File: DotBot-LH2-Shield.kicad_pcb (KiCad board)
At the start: 4 copper layers, 29 x 27 mm, 23 parts, among them J1 Conn_01x04, J2 Conn_01x10, J3 Conn_01x10, Q1 NX6008NBKWX, Q2 NX6008NBKWX, Q3 NX6008NBKWX, U1 ISM330DHCXTR, U2 TS4231, U4 LIS3MDL

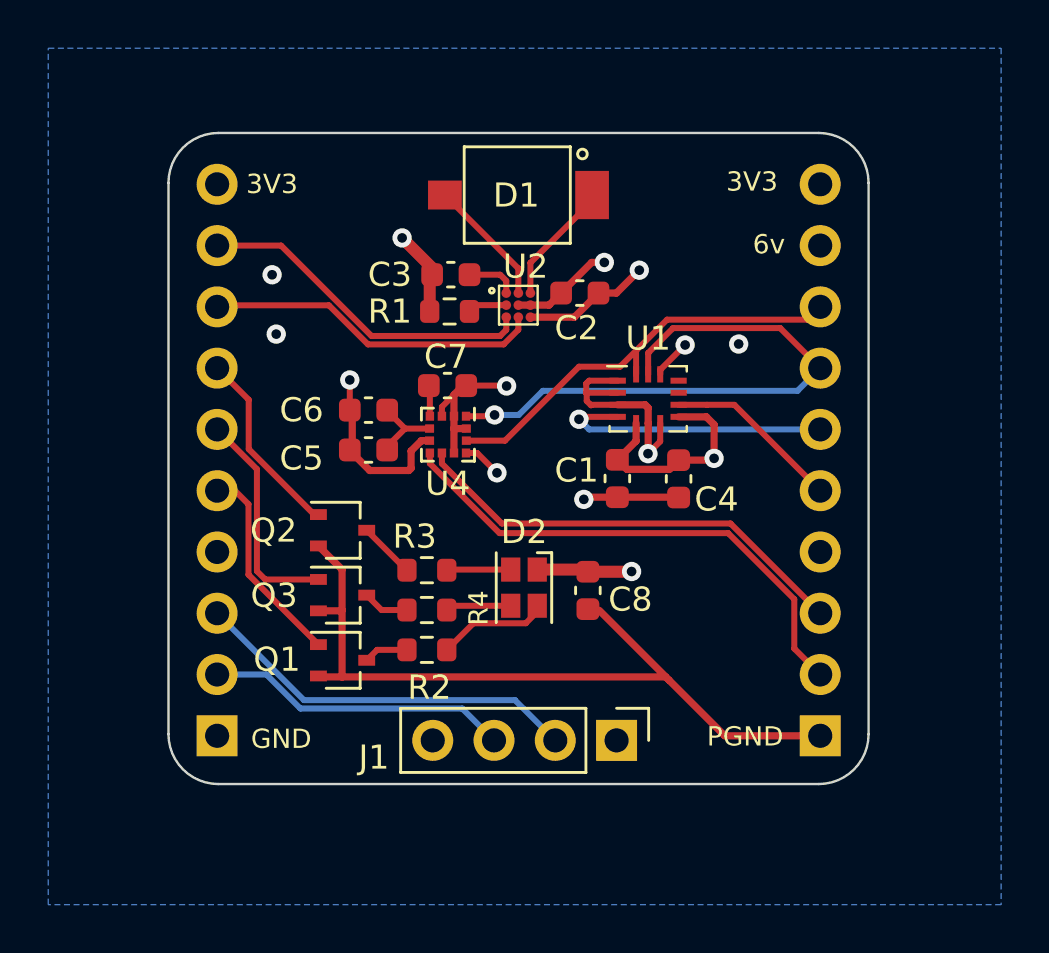
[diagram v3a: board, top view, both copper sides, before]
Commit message: DotBot-LH2-Shield: cleanup silkscreen labels, remove remaining useless stitching vias
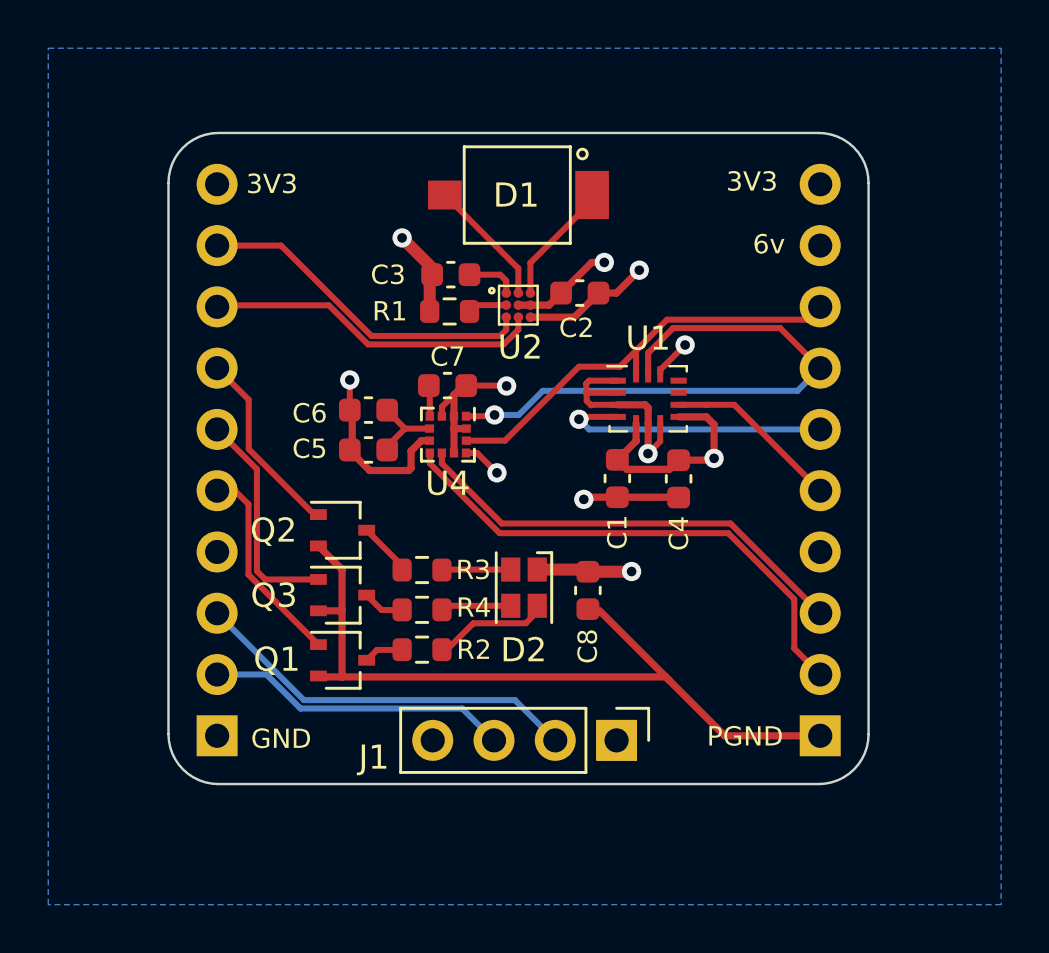
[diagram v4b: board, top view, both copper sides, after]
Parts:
- moved R4 0.20 mm to (138.5, 117.8)
- moved R2 0.20 mm to (138.5, 119.4)
- moved R3 0.20 mm to (138.5, 116.1)
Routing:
- net GND: vias 8 -> 5
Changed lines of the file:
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@@
   (net 32 "DRDY")
   (footprint "Resistor_SMD:R_0603_1608Metric" (layer "F.Cu")
-    (at 138.695 116.136)
+    (at 138.495 116.128)
     (descr "Resistor SMD 0603 (1608 Metric), square (rectangular) end terminal, IPC_7351 nominal, (Body size source: IPC-SM-782 page 72, https://www.pcb-3d.com/wordpress/wp-content/uploads/ipc-sm-782a_amendment_1_and_2.pdf), generated with kicad-footprint-generator")
     (tags "resistor")
@@
     (property "ki_keywords" "R res resistor")
     (attr smd)
-    (fp_text reference "R3" (at -0.505 -1.396) (layer "F.SilkS")
-        (effects (font (size 1 1) (thickness 0.15)))
+    (fp_text reference "R3" (at 2.125 0.004 180) (layer "F.SilkS")
+        (effects (font (size 0.8 0.8) (thickness 0.15)))
     )
     (fp_text value "750" (at 0 1.43) (layer "F.Fab")
@@
   )
   (footprint "Resistor_SMD:R_0603_1608Metric" (layer "F.Cu")
-    (at 138.695 117.787)
+    (at 138.495 117.779)
     (descr "Resistor SMD 0603 (1608 Metric), square (rectangular) end terminal, IPC_7351 nominal, (Body size source: IPC-SM-782 page 72, https://www.pcb-3d.com/wordpress/wp-content/uploads/ipc-sm-782a_amendment_1_and_2.pdf), generated with kicad-footprint-generator")
     (tags "resistor")
@@
     (property "ki_keywords" "R res resistor")
     (attr smd)
-    (fp_text reference "R4" (at 2.145 -0.087 270) (layer "F.SilkS")
+    (fp_text reference "R4" (at 2.145 -0.087) (layer "F.SilkS")
         (effects (font (size 0.8 0.8) (thickness 0.15)))
     )
@@
     (property "ki_description" "2nd Generation Light to Digital Converter (Envelope and Data)")
     (attr smd)
-    (fp_text reference "U2" (at 0.3 -1.6) (layer "F.SilkS")
+    (fp_text reference "U2" (at 0.084 1.752) (layer "F.SilkS")
         (effects (font (size 1 1) (thickness 0.15)))
     )
@@
     (property "ki_keywords" "cap capacitor")
     (attr smd)
-    (fp_text reference "C8" (at 0.375 -1.76 -180) (layer "F.SilkS")
-        (effects (font (size 1 1) (thickness 0.15)))
+    (fp_text reference "C8" (at 2.315 0 -90) (layer "F.SilkS")
+        (effects (font (size 0.8 0.8) (thickness 0.15)))
     )
     (fp_text value "100nF" (at 0 1.43 90) (layer "F.Fab")
@@
     (attr smd)
     (fp_text reference "C2" (at -0.134 1.452) (layer "F.SilkS")
-        (effects (font (size 1 1) (thickness 0.15)))
+        (effects (font (size 0.8 0.8) (thickness 0.15)))
     )
     (fp_text value "100nF" (at 0 1.43) (layer "F.Fab")
@@
     (attr smd)
     (fp_text reference "R1" (at -2.477 0) (layer "F.SilkS")
-        (effects (font (size 1 1) (thickness 0.15)))
+        (effects (font (size 0.8 0.8) (thickness 0.15)))
     )
     (fp_text value "15k" (at -33.83 17.18) (layer "F.Fab")
@@
     (property "ki_keywords" "cap capacitor")
     (attr smd)
-    (fp_text reference "C1" (at -0.3355 1.69 -180) (layer "F.SilkS")
-        (effects (font (size 1 1) (thickness 0.15)))
+    (fp_text reference "C1" (at 2.2245 -0.01 -90) (layer "F.SilkS")
+        (effects (font (size 0.8 0.8) (thickness 0.15)))
     )
     (fp_text value "100nF" (at 0 1.43 90) (layer "F.Fab")
@@
   (footprint "LED_SMD:LED_Cree-PLCC4_2x2mm_CW" (layer "F.Cu")
     (at 142.72 116.86 -90)
-    (descr "2.0mm x 2.0mm PLCC4 LED, http://www.cree.com/~/media/Files/Cree/LED-Components-and-Modules/HB/Data-Sheets/CLMVBFKA.pdf")
-    (tags "LED Cree PLCC-4")
+    (descr "2.0mm x 2.0mm PLCC4 LED, https://assets.cree-led.com/a/ds/h/HB-CLMVC-FKA.pdf")
+    (tags "LED Cree PLCC-4 2020 CLMVB-FKA CLMVC-FKA")
     (property "Link" "https://www.digikey.fr/short/ppj3nqm1")
     (property "Mfr Part Number" "CLMVC-FKA")
@@
     (property "ki_keywords" "LED RGB diode")
     (attr smd)
-    (fp_text reference "D2" (at -2.313 -0.004) (layer "F.SilkS")
+    (fp_text reference "D2" (at 2.59 0.01) (layer "F.SilkS")
         (effects (font (size 1 1) (thickness 0.15)))
     )
@@
     (pad "4" smd rect (at -0.75 0.55 270) (size 1 0.8) (layers "F.Cu" "F.Paste" "F.Mask")
       (net 19 "Net-(D2-GK)") (pinfunction "GK") (pintype "passive"))
-    (model "${KICAD6_3DMODEL_DIR}/LED_SMD.3dshapes/LED_Cree-PLCC4_2x2mm_CW.wrl"
+    (model "${KICAD7_3DMODEL_DIR}/LED_SMD.3dshapes/LED_Cree-PLCC4_2x2mm_CW.wrl"
       (offset (xyz 0 0 0))
       (scale (xyz 1 1 1))
@@
   )
   (footprint "Resistor_SMD:R_0603_1608Metric" (layer "F.Cu")
-    (at 138.695 119.438)
+    (at 138.495 119.43)
     (descr "Resistor SMD 0603 (1608 Metric), square (rectangular) end terminal, IPC_7351 nominal, (Body size source: IPC-SM-782 page 72, https://www.pcb-3d.com/wordpress/wp-content/uploads/ipc-sm-782a_amendment_1_and_2.pdf), generated with kicad-footprint-generator")
     (tags "resistor")
@@
     (property "ki_keywords" "R res resistor")
     (attr smd)
-    (fp_text reference "R2" (at 0.105 1.562) (layer "F.SilkS")
-        (effects (font (size 1 1) (thickness 0.15)))
+    (fp_text reference "R2" (at 2.155 0.012 180) (layer "F.SilkS")
+        (effects (font (size 0.8 0.8) (thickness 0.15)))
     )
     (fp_text value "1k" (at 0 1.43) (layer "F.Fab")
@@
     (property "ki_keywords" "cap capacitor")
     (attr smd)
-    (fp_text reference "C3" (at -2.527 0) (layer "F.SilkS")
-        (effects (font (size 1 1) (thickness 0.15)))
+    (fp_text reference "C3" (at -2.597 0.014) (layer "F.SilkS")
+        (effects (font (size 0.8 0.8) (thickness 0.15)))
     )
     (fp_text value "1uF" (at 0 1.43) (layer "F.Fab")
@@
     (property "ki_keywords" "cap capacitor")
     (attr smd)
-    (fp_text reference "C4" (at 0.8515 -1.57 -180) (layer "F.SilkS")
-        (effects (font (size 1 1) (thickness 0.15)))
+    (fp_text reference "C4" (at 2.2615 -0.02 90) (layer "F.SilkS")
+        (effects (font (size 0.8 0.8) (thickness 0.15)))
     )
     (fp_text value "100nF" (at 0 1.43 90) (layer "F.Fab")
@@
     (property "ki_keywords" "cap capacitor")
     (attr smd)
-    (fp_text reference "C6" (at -2.775 0) (layer "F.SilkS")
-        (effects (font (size 1 1) (thickness 0.15)))
+    (fp_text reference "C6" (at -2.435 0.14) (layer "F.SilkS")
+        (effects (font (size 0.8 0.8) (thickness 0.15)))
     )
     (fp_text value "1uF" (at 0 1.43) (layer "F.Fab")
@@
     (property "ki_keywords" "cap capacitor")
     (attr smd)
-    (fp_text reference "C5" (at -2.775 0.349 180) (layer "F.SilkS")
-        (effects (font (size 1 1) (thickness 0.15)))
+    (fp_text reference "C5" (at -2.435 -0.041 180) (layer "F.SilkS")
+        (effects (font (size 0.8 0.8) (thickness 0.15)))
     )
     (fp_text value "100nF" (at 0 1.43) (layer "F.Fab")
@@
     (property "ki_keywords" "cap capacitor")
     (attr smd)
-    (fp_text reference "C7" (at -0.06 -1.2) (layer "F.SilkS")
-        (effects (font (size 1 1) (thickness 0.15)))
+    (fp_text reference "C7" (at 0.009 -1.194) (layer "F.SilkS")
+        (effects (font (size 0.8 0.8) (thickness 0.15)))
     )
     (fp_text value "100nF" (at 0 1.43) (layer "F.Fab")
@@
   (segment (start 140.3305 110.2655) (end 139.843 110.2655) (width 0.3) (layer "F.Cu") (net 1))
   (segment (start 139.818 108.865) (end 139.818 109.753) (width 0.3) (layer "F.Cu") (net 1))
-  (segment (start 148.73 120.69) (end 151.04 123) (width 0.3) (layer "F.Cu") (net 1))
   (segment (start 145.32 108.78) (end 146.605 108.78) (width 0.25) (layer "F.Cu") (net 1))
   (segment (start 148.3675 110.0425) (end 148.3675 110.7975) (width 0.25) (layer "F.Cu") (net 1))
   (segment (start 139.318 109.753) (end 139.318 109.365) (width 0.25) (layer "F.Cu") (net 1))
   (segment (start 139.318 109.365) (end 139.818 108.865) (width 0.25) (layer "F.Cu") (net 1))
+  (segment (start 151.04 123) (end 148.73 120.69) (width 0.3) (layer "F.Cu") (net 1))
   (segment (start 139.843 110.2655) (end 139.818 110.2405) (width 0.3) (layer "F.Cu") (net 1))
   (segment (start 145.42 108.28) (end 145.3 108.4) (width 0.25) (layer "F.Cu") (net 1))
@@
   (via (at 146.05 103.378) (size 0.8) (drill 0.4) (layers "F.Cu" "B.Cu") (net 1))
   (via (at 142 108.5) (size 0.8) (drill 0.4) (layers "F.Cu" "B.Cu") (net 1))
-  (via (at 132.45 106.35) (size 0.8) (drill 0.4) (layers "F.Cu" "B.Cu") (free) (net 1))
-  (via (at 151.62 106.76) (size 0.8) (drill 0.4) (layers "F.Cu" "B.Cu") (free) (net 1))
   (via (at 145.2 113.2) (size 0.8) (drill 0.4) (layers "F.Cu" "B.Cu") (net 1))
   (via (at 137.668 102.362) (size 0.8) (drill 0.4) (layers "F.Cu" "B.Cu") (net 1))
   (via (at 147.86 111.305) (size 0.8) (drill 0.4) (layers "F.Cu" "B.Cu") (net 1))
-  (via (at 132.28 103.89) (size 0.8) (drill 0.4) (layers "F.Cu" "B.Cu") (free) (net 1))
   (segment (start 146.984 111.9545) (end 148.749 111.9545) (width 0.3) (layer "F.Cu") (net 2))
   (segment (start 140.318 111.278) (end 140.778 111.278) (width 0.25) (layer "F.Cu") (net 2))

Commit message: Increase min trace spacing from 0.1mm to 0.15mm
To better fit with Eurocircuit fabrication guidelines
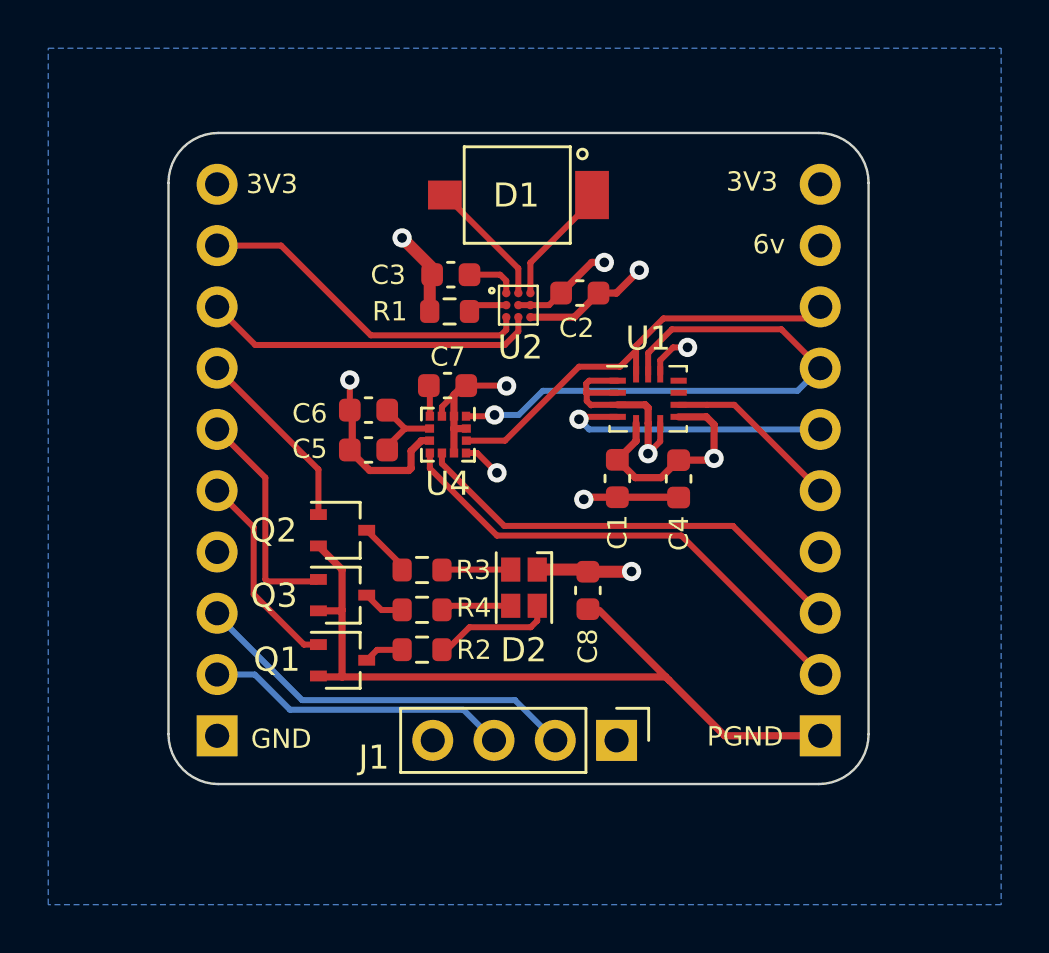
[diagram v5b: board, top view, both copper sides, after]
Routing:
- net INT: track 21.4 -> 20.4 mm
- net +3V3: track 25.1 -> 25.7 mm
